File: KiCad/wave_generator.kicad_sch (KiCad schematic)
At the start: 10 parts, among them U4 MCP6002-xP

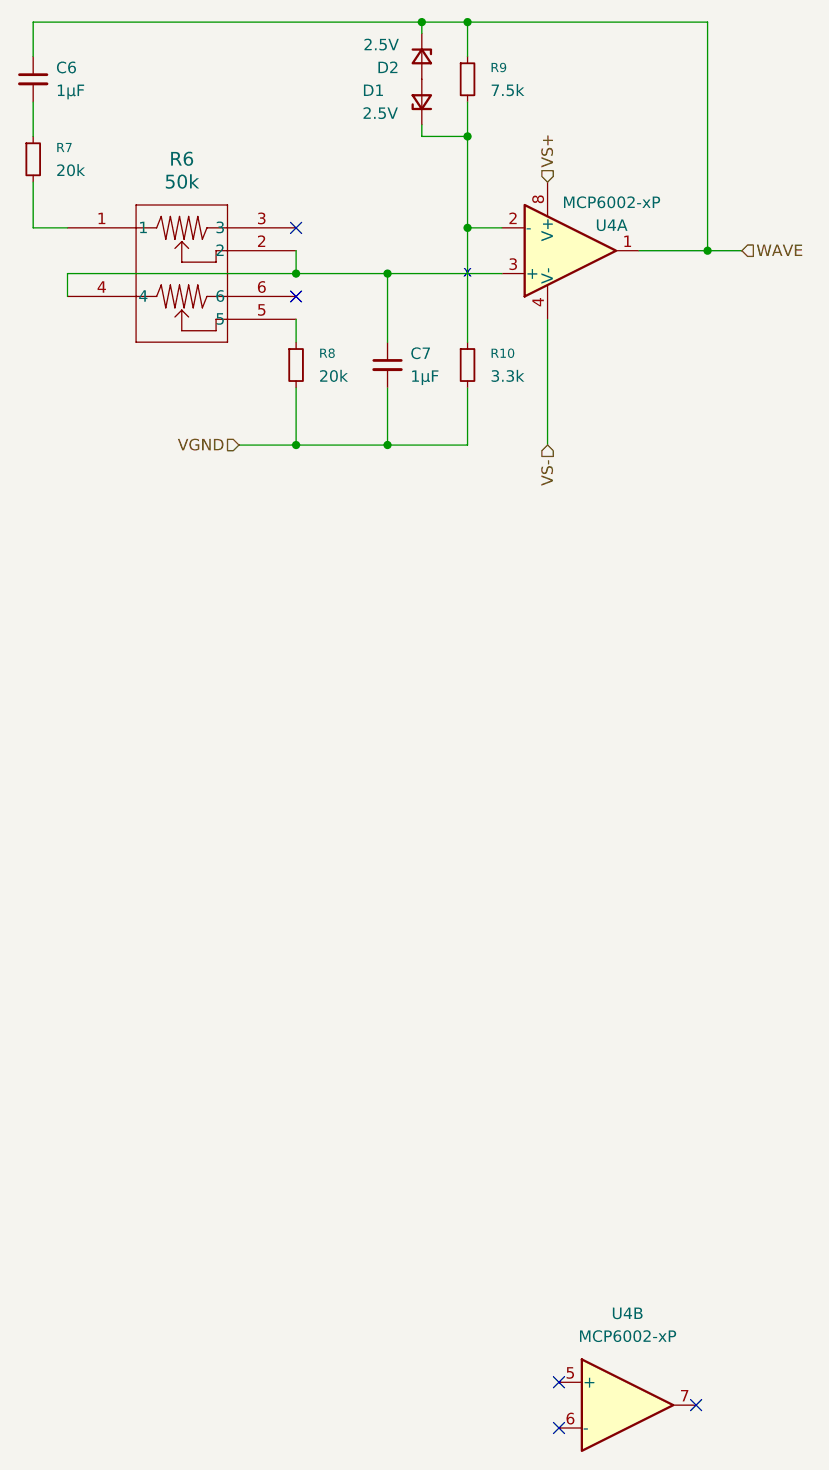
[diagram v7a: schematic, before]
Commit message: Some TP -> Headers, added footprints, fixed battery footprint, started layout of board.
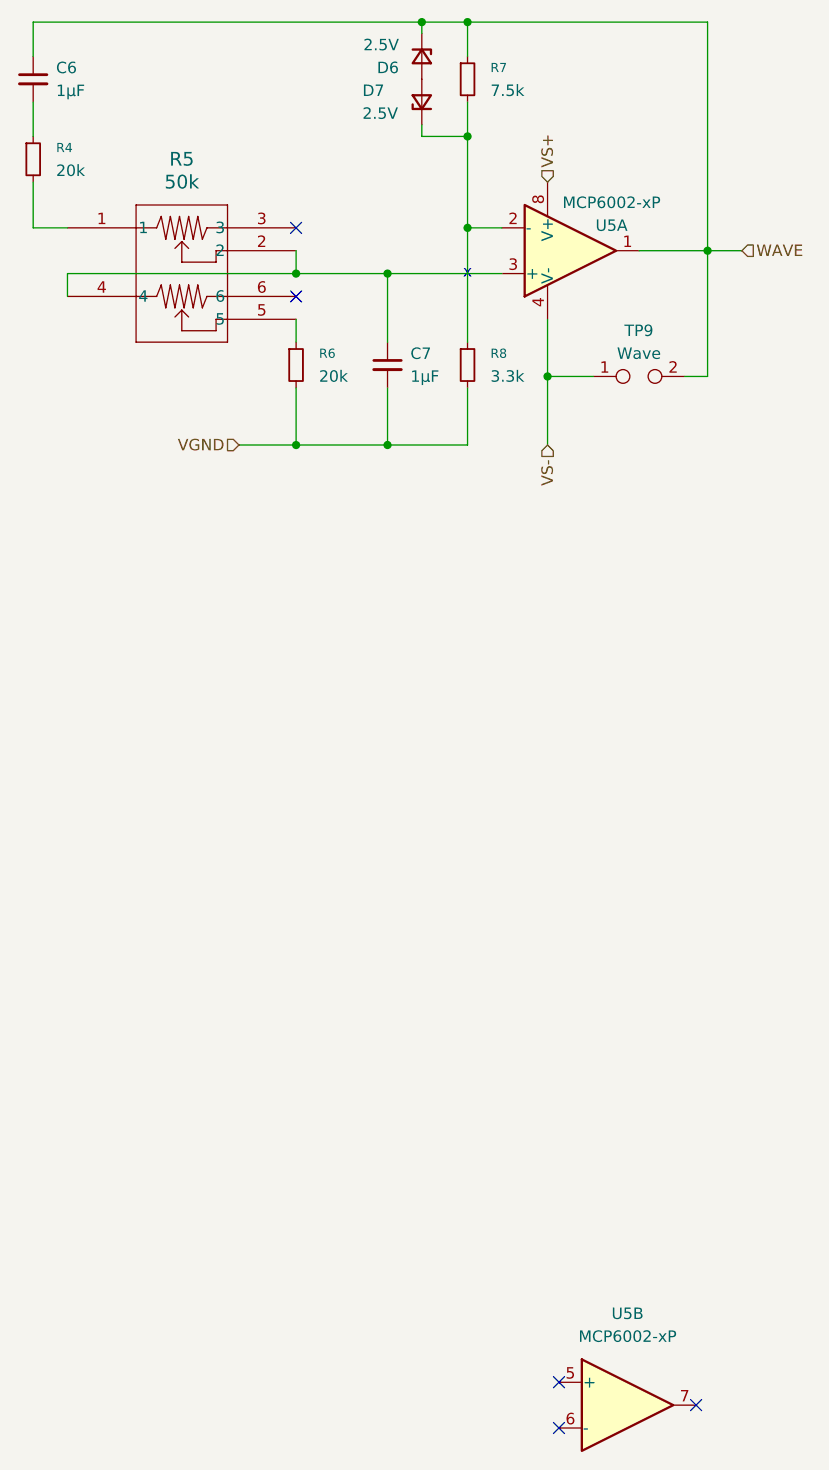
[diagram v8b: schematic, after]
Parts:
- added TP9: Wave, Connector_PinSocket_2.54mm:PinSocket_1x02_P2.54mm_Vertical, symbol Connector:TestPoint_2Pole
- U5: renamed from U4; footprint (none) -> Package_DIP:DIP-8_W7.62mm
- renumbered D2 to D6, D1 to D7, R7 to R4, R6 to R5, R8 to R6, R9 to R7, R10 to R8
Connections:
- net VS-: now also TP9.1
- net WAVE: now also TP9.2
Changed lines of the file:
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@@
 	)
 	(junction
+		(at 116.84 63.5)
+		(diameter 0)
+		(color 0 0 0 0)
+	)
+	(junction
 		(at 99.06 52.07)
 		(diameter 0)
@@
 	(wire
 		(pts
-			(xy 116.84 71.12) (xy 116.84 57.15)
+			(xy 116.84 71.12) (xy 116.84 63.5)
+		)
+		(stroke
+			(width 0)
+			(type default)
+		)
+	)
+	(wire
+		(pts
+			(xy 134.62 49.53) (xy 134.62 63.5)
 		)
 		(stroke
@@
 	(wire
 		(pts
+			(xy 134.62 63.5) (xy 132.08 63.5)
+		)
+		(stroke
+			(width 0)
+			(type default)
+		)
+	)
+	(wire
+		(pts
 			(xy 82.55 71.12) (xy 88.9 71.12)
 		)
@@
 	(wire
 		(pts
+			(xy 116.84 63.5) (xy 116.84 57.15)
+		)
+		(stroke
+			(width 0)
+			(type default)
+		)
+	)
+	(wire
+		(pts
 			(xy 102.87 24.13) (xy 107.95 24.13)
 		)
@@
 	(wire
 		(pts
+			(xy 116.84 63.5) (xy 121.92 63.5)
+		)
+		(stroke
+			(width 0)
+			(type default)
+		)
+	)
+	(wire
+		(pts
 			(xy 134.62 49.53) (xy 134.62 24.13)
 		)
@@
 			"VlR1bDFldE9lZDRYb0thN295R1lYeisrZWRISEhFRXZoQndyR1ZaVUV4MUVWUXB0V1BIanE1ZHU5"
 			"YkRXenBiNG56ZUYvV1RkbktuIgoiejJqSXJqWG5hQTZGS2s4Qnl5WTltTWgrZUxYcDB4U3dvVStB"
-			"VU9udUtKUTQ0NnNLelVaRnVxblFEUzFnZjFYdno2ZU1oNGNvU0NIeiIKIkVSVA=="
+			"VU9udUtKUTQ0NnNLelVaRnVxblFEUzFnZjFYdno2ZU1oNGNvU0NIeiIKIkVSVABIAHkAYwBrAGoA"
+			"UABXAGYAcAAvAFAAbgB6AEwANwAzADAAVQBrADMANABlAEcATABPAFMAMABxAFYAWgBXADgATQBF"
+			"AFkAMABuAE4AMgBnAE8AZwBwAE4AdwB6AGQAWgBQAFcASwBQAGcAMAAxAFoAZABYAFMAMQA5ADAA"
+			"agBtAHcAZQBaAG8ASgBiAEsAdgBTAFoAaABhAHgAWABTAGsAdABXAFgAeABsAHQAcQAvAHoAZQB2"
+			"AG0AaABUAEsASwBiAEUAVABCAFEAMABvAGEAaQBSAEUAMQBLAGkAaABHAG4AdgBJAEwAeQA3AEQA"
+			"UQB2AGMAdABXAGoAVwBkAGwAaAAxAC8ASABPAEIAWQBBAEoAVQAxAFIAVQBSAEsAZgA0AGoASABZ"
+			"AHgAZAAxAE4AdwBVAFMAdQBRAEYAZwBMAHYAMABrAEEAVwBVAGgAcABuAGwAeQB4AFoAWQBoAGoA"
+			"RwBCAFIAZABjAG8ASwB3AHkATgB2AGYAZQBlAHkAOQBxACsAMABGAGEASgBoAEsASgBrAHAASQBT"
+			"AEcAUwBFADAAZAArADcAYwBWAEMAbwAxAGQAZQBwAFUAYQBuADMAOABtAFUAMAB3ADEAbQBnAHYA"
+			"egBmADgAQgBuAFUAMQBSAG4AdQBjAFAAcQBkADMAQgBLAEoAZABLAHAAYgBCAHkAegB6ADMAMwAz"
+			"AEMAVgBMAGwAaQBpAGgAZwBYAHoAMwAzAFgAZABkAHUAbgBTAHgAMABVAEoAMQBmAGkAbgBVAFoA"
+			"TgBEAHQAOQB1ADMAYgBsADUAZQBYADgAMQA0AC8ALwBQAEEARAB0AG0AWgAwAFIAdAA0AEMAYwBS"
+			"AFUAMgBUAFoAdABiAEwAYQBOAHoAYwBBAEQAMwBlAHIAMAAyAGgAeQAyAE8AbQAzAE8AVAAzAFgA"
+			"ZABhAEMARABZAGwAWABJAGIAbgBvAHUAOAB5AG8ANgBKAEoAaABFAEQATgBsAGwAUwBjAFYAcABO"
+			"ADcATQBiAGQAeQB6AFEASwBQAEcARABsADYAMQBmAGkAUQArAGcALwBWAEIAbwB3AC8AUwB2AGgA"
+			"dwBWAEcAWAAxAGgANAB5AFEAbwA2AFMAVQBLAGkAdwBzAGoARQBRAGkAcABoAFcANgBoADMAaAA2"
+			"AFAAagBoAEgARAA1AFAAWgBwAGcAZABTAG4AKwBRADcASQBwAEUAVABpAFUAVAAyAGgAUgBiAEMA"
+			"cgBLAFAAdQBIAFkAMQBHAFEAVAB0AGwAdQB6ADYAagAvAFYAQwBxAGQAbgB3ADAASABoAFoAcQAy"
+			"ADYAVQBtAGgARQBzAEwATgBUADIAawBtAE8ATgBFADEAQwB6AEgAVQBwAG8AVg=="
 		)
 	)
@@
 		(dnp no)
 		(fields_autoplaced yes)
-		(property "Reference" "U4"
+		(property "Reference" "U5"
 			(at 118.11 48.2599 0)
 			(effects
@@
 			)
 		)
-		(property "Footprint" ""
+		(property "Footprint" "Package_DIP:DIP-8_W7.62mm"
 			(at 119.38 49.53 0)
 			(effects
@@
 			(project ""
 				(path "/57b9e980-cd8f-44e4-af61-2cbd5bb30325/bb283dc1-1993-4617-8bcd-6a423451a748"
-					(reference "U4")
+					(reference "U5")
 					(unit 3)
 				)
@@
 		(dnp no)
 		(fields_autoplaced yes)
-		(property "Reference" "U4"
+		(property "Reference" "U5"
 			(at 125.73 167.64 0)
 			(effects
@@
 			)
 		)
-		(property "Footprint" ""
+		(property "Footprint" "Package_DIP:DIP-8_W7.62mm"
 			(at 125.73 177.8 0)
 			(effects
@@
 			(project ""
 				(path "/57b9e980-cd8f-44e4-af61-2cbd5bb30325/bb283dc1-1993-4617-8bcd-6a423451a748"
-					(reference "U4")
+					(reference "U5")
 					(unit 2)
 				)
@@
 		(dnp no)
 		(fields_autoplaced yes)
-		(property "Reference" "R6"
+		(property "Reference" "R5"
 			(at 76.2 39.37 0)
 			(effects
@@
 			(project ""
 				(path "/57b9e980-cd8f-44e4-af61-2cbd5bb30325/bb283dc1-1993-4617-8bcd-6a423451a748"
-					(reference "R6")
+					(reference "R5")
 					(unit 1)
 				)
@@
 		(on_board yes)
 		(dnp no)
-		(property "Reference" "U4"
+		(property "Reference" "U5"
 			(at 123.952 46.736 0)
 			(effects
@@
 			)
 		)
-		(property "Footprint" ""
+		(property "Footprint" "Package_DIP:DIP-8_W7.62mm"
 			(at 119.38 49.53 0)
 			(effects
@@
 			(project ""
 				(path "/57b9e980-cd8f-44e4-af61-2cbd5bb30325/bb283dc1-1993-4617-8bcd-6a423451a748"
-					(reference "U4")
+					(reference "U5")
 					(unit 1)
 				)
@@
 		(on_board yes)
 		(dnp no)
-		(property "Reference" "D2"
+		(property "Reference" "D6"
 			(at 100.33 29.2101 90)
 			(effects
@@
 			(project "ChipTester_354"
 				(path "/57b9e980-cd8f-44e4-af61-2cbd5bb30325/bb283dc1-1993-4617-8bcd-6a423451a748"
-					(reference "D2")
+					(reference "D6")
 					(unit 1)
 				)
@@
 		(dnp no)
 		(fields_autoplaced yes)
-		(property "Reference" "R9"
+		(property "Reference" "R7"
 			(at 110.49 29.2099 0)
 			(effects
@@
 			(project "ChipTester_354"
 				(path "/57b9e980-cd8f-44e4-af61-2cbd5bb30325/bb283dc1-1993-4617-8bcd-6a423451a748"
-					(reference "R9")
+					(reference "R7")
 					(unit 1)
 				)
@@
 		(dnp no)
 		(fields_autoplaced yes)
-		(property "Reference" "R8"
+		(property "Reference" "R6"
 			(at 91.44 60.9599 0)
 			(effects
@@
 			(project "ChipTester_354"
 				(path "/57b9e980-cd8f-44e4-af61-2cbd5bb30325/bb283dc1-1993-4617-8bcd-6a423451a748"
-					(reference "R8")
+					(reference "R6")
+					(unit 1)
+				)
+			)
+		)
+	)
+	(symbol
+		(lib_id "Connector:TestPoint_2Pole")
+		(at 127 63.5 0)
+		(unit 1)
+		(exclude_from_sim no)
+		(in_bom yes)
+		(on_board yes)
+		(dnp no)
+		(fields_autoplaced yes)
+		(property "Reference" "TP9"
+			(at 127 58.42 0)
+			(effects
+				(font
+					(size 1.27 1.27)
+				)
+			)
+		)
+		(property "Value" "Wave"
+			(at 127 60.96 0)
+			(effects
+				(font
+					(size 1.27 1.27)
+				)
+			)
+		)
+		(property "Footprint" "Connector_PinSocket_2.54mm:PinSocket_1x02_P2.54mm_Vertical"
+			(at 127 63.5 0)
+			(effects
+				(font
+					(size 1.27 1.27)
+				)
+				(hide yes)
+			)
+		)
+		(property "Datasheet" "~"
+			(at 127 63.5 0)
+			(effects
+				(font
+					(size 1.27 1.27)
+				)
+				(hide yes)
+			)
+		)
+		(property "Description" "2-polar test point"
+			(at 127 63.5 0)
+			(effects
+				(font
+					(size 1.27 1.27)
+				)
+				(hide yes)
+			)
+		)
+		(pin "1"
+		)
+		(pin "2"
+		)
+		(instances
+			(project ""
+				(path "/57b9e980-cd8f-44e4-af61-2cbd5bb30325/bb283dc1-1993-4617-8bcd-6a423451a748"
+					(reference "TP9")
 					(unit 1)
 				)
@@
 		(dnp no)
 		(fields_autoplaced yes)
-		(property "Reference" "R10"
+		(property "Reference" "R8"
 			(at 110.49 60.9599 0)
 			(effects
@@
 			(project "ChipTester_354"
 				(path "/57b9e980-cd8f-44e4-af61-2cbd5bb30325/bb283dc1-1993-4617-8bcd-6a423451a748"
-					(reference "R10")
+					(reference "R8")
 					(unit 1)
 				)
@@
 		(dnp no)
 		(fields_autoplaced yes)
-		(property "Reference" "R7"
+		(property "Reference" "R4"
 			(at 62.23 38.0999 0)
 			(effects
@@
 			(project ""
 				(path "/57b9e980-cd8f-44e4-af61-2cbd5bb30325/bb283dc1-1993-4617-8bcd-6a423451a748"
-					(reference "R7")
+					(reference "R4")
 					(unit 1)
 				)
@@
 		(on_board yes)
 		(dnp no)
-		(property "Reference" "D1"
+		(property "Reference" "D7"
 			(at 96.266 31.75 90)
 			(effects
@@
 			(project ""
 				(path "/57b9e980-cd8f-44e4-af61-2cbd5bb30325/bb283dc1-1993-4617-8bcd-6a423451a748"
-					(reference "D1")
+					(reference "D7")
 					(unit 1)
 				)
